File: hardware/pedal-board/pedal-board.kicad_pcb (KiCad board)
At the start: 2 copper layers, 108 x 64 mm, 50 parts, among them J1 AudioJack0, J10 CH7, J11 CH7, J12 Qwiic, J13 Qwiic, J2 AudioJack1, J3 AudioJack2, J4 AudioJack3, J5 Qwiic, J6 CH7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

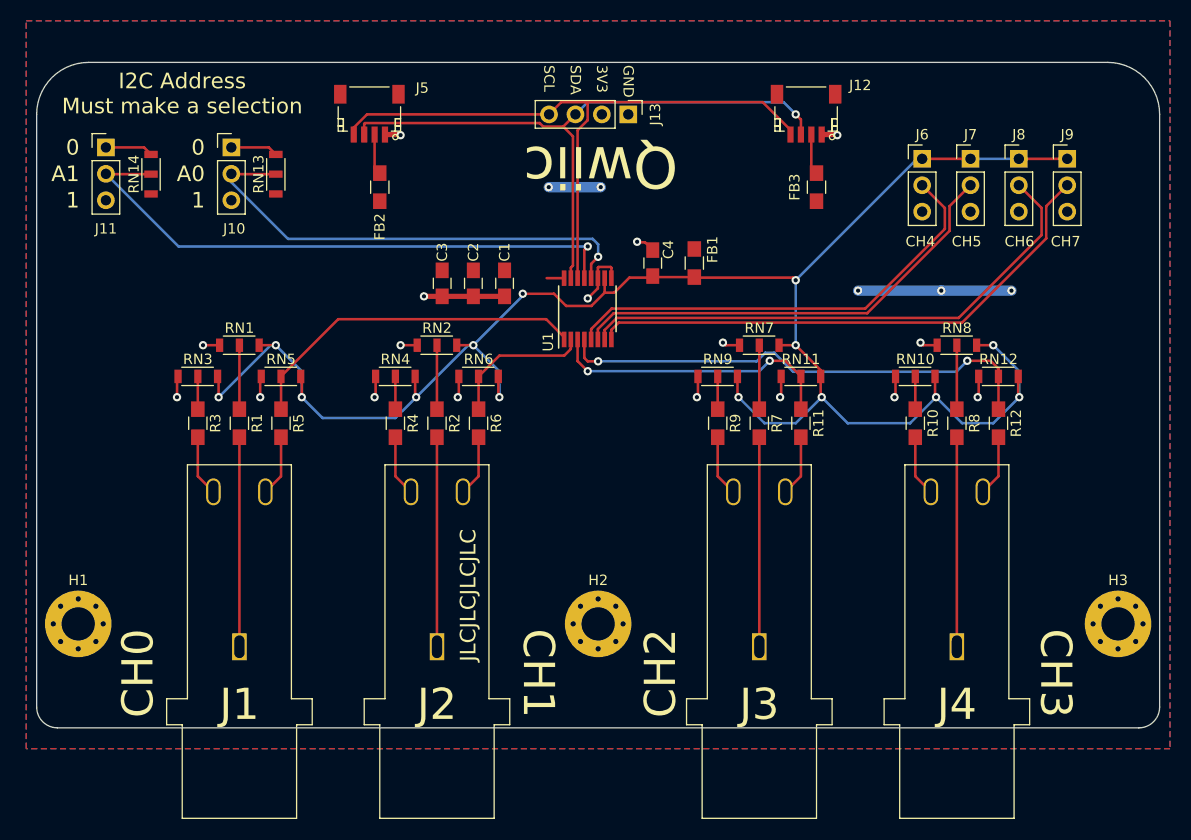
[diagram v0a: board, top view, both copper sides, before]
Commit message: Made changes for pedal board rev 2, per issue #40
* 1uF caps on all the incoming signal lines
* Switched to STM32G0 from the I2C ADC
* Added IRQ support, with transistor for pull down
* Every TRS pin is brought to an ADC pin, so we can attempt autodetection
  of pedal behavior.
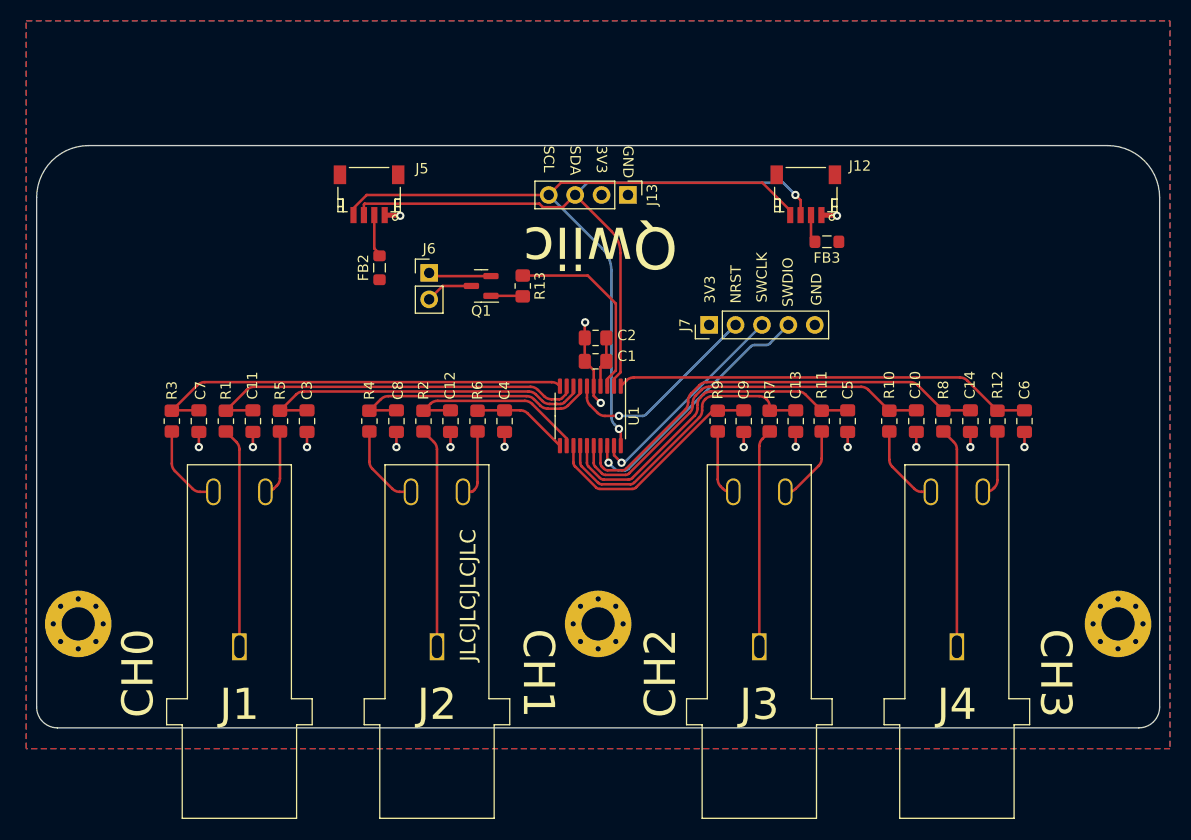
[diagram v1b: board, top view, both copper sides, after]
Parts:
- removed FB1: FB, Inductors_SMD:L_0805_HandSoldering
- removed J10, J11, J8, J9: CH7, Pin_Headers:Pin_Header_Straight_1x03_Pitch2.54mm
- removed RN1, RN10, RN11, RN12, RN13, RN14, RN2, RN3, RN4, RN5, RN6, RN7, RN8, RN9: Div, footprints:R_0805_Divider
- added C10: 1uF, Capacitor_SMD:C_0805_2012Metric_Pad1.18x1.45mm_HandSolder, F.Cu at (100.6, 68.5)
- added C11: 1uF, Capacitor_SMD:C_0805_2012Metric_Pad1.18x1.45mm_HandSolder, F.Cu at (36.8, 68.5)
- added C12: 1uF, Capacitor_SMD:C_0805_2012Metric_Pad1.18x1.45mm_HandSolder, F.Cu at (55.8, 68.5)
- added C13: 1uF, Capacitor_SMD:C_0805_2012Metric_Pad1.18x1.45mm_HandSolder, F.Cu at (89.0, 68.5)
- added C14: 1uF, Capacitor_SMD:C_0805_2012Metric_Pad1.18x1.45mm_HandSolder, F.Cu at (105.8, 68.5)
- added C5: 1uF, Capacitor_SMD:C_0805_2012Metric_Pad1.18x1.45mm_HandSolder, F.Cu at (94.0, 68.5)
- added C6: 1uF, Capacitor_SMD:C_0805_2012Metric_Pad1.18x1.45mm_HandSolder, F.Cu at (111.0, 68.5)
- added C7: 1uF, Capacitor_SMD:C_0805_2012Metric_Pad1.18x1.45mm_HandSolder, F.Cu at (31.6, 68.5)
- added C8: 1uF, Capacitor_SMD:C_0805_2012Metric_Pad1.18x1.45mm_HandSolder, F.Cu at (50.6, 68.5)
- added C9: 1uF, Capacitor_SMD:C_0805_2012Metric_Pad1.18x1.45mm_HandSolder, F.Cu at (84.0, 68.5)
- added Q1: Q_NPN_BEC, Package_TO_SOT_SMD:SOT-23, F.Cu at (58.8, 55.5)
- added R13: 10k, Resistor_SMD:R_0805_2012Metric_Pad1.20x1.40mm_HandSolder, F.Cu at (62.8, 55.5)
- C1: footprint Capacitors_SMD:C_0805_HandSoldering -> Capacitor_SMD:C_0805_2012Metric_Pad1.18x1.45mm_HandSolder
- C2: value 1uF -> 4.7uF; footprint Capacitors_SMD:C_0805_HandSoldering -> Capacitor_SMD:C_0805_2012Metric_Pad1.18x1.45mm_HandSolder
- C3: value 4.7uF -> 1uF; footprint Capacitors_SMD:C_0805_HandSoldering -> Capacitor_SMD:C_0805_2012Metric_Pad1.18x1.45mm_HandSolder
- C4: value 0.1uF -> 1uF; footprint Capacitors_SMD:C_0805_HandSoldering -> Capacitor_SMD:C_0805_2012Metric_Pad1.18x1.45mm_HandSolder
- FB2, FB3: footprint Inductors_SMD:L_0805_HandSoldering -> Inductor_SMD:L_0805_2012Metric_Pad1.05x1.20mm_HandSolder
- J13: footprint Pin_Headers:Pin_Header_Straight_1x04_Pitch2.54mm -> Connector_PinHeader_2.54mm:PinHeader_1x04_P2.54mm_Vertical
- J6: value CH7 -> IRQ; footprint Pin_Headers:Pin_Header_Straight_1x03_Pitch2.54mm -> Connector_PinHeader_2.54mm:PinHeader_1x02_P2.54mm_Vertical
- J7: value CH7 -> Serial Wire Debug; footprint Pin_Headers:Pin_Header_Straight_1x03_Pitch2.54mm -> Connector_PinHeader_2.54mm:PinHeader_1x05_P2.54mm_Vertical
- R1, R10, R11, R12, R2, R3, R4, R5, R6, R7, R8, R9: footprint Resistors_SMD:R_0805_HandSoldering -> Resistor_SMD:R_0805_2012Metric_Pad1.20x1.40mm_HandSolder
- U1: value ADS7830 -> STM32G030Fx; footprint Housings_SSOP:TSSOP-16_4.4x5mm_Pitch0.65mm -> Package_SO:TSSOP-20_4.4x6.5mm_P0.65mm
- moved J6 48.7 mm to (53.8, 54.2)
- moved J7 29.8 mm to (80.7, 59.2), turned to 90 degrees
- moved C4 20.8 mm to (61.0, 68.5), turned to -90 degrees
- moved C3 18.6 mm to (42.0, 68.5)
- moved C2 12.9 mm to (69.8, 60.5), turned to 180 degrees
- moved C1 11.5 mm to (69.8, 62.8), turned to 180 degrees
- moved U1 10.3 mm to (69.2, 68.0), turned to -90 degrees
- moved FB2 7.75 mm to (49.0, 53.8)
- moved J12 7.75 mm to (90.0, 46.8)
- moved J13 7.75 mm to (72.9, 46.8)
- moved J5 7.75 mm to (48.0, 46.8)
- moved FB3 5.34 mm to (92.0, 51.2), turned to 180 degrees
- moved R10 2.51 mm to (98.0, 68.5)
- moved R3 2.51 mm to (29.0, 68.5)
- moved R4 2.51 mm to (48.0, 68.5)
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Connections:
- net Net-(J7-Pad2) renamed /NRST
- C3 pad 1: +3V3 -> /J1_T
- C4 pad 1: +3.3VA -> /J2_T
- J6 pad 1: +3.3VA -> GND
- J7 pad 1: +3.3VA -> +3V3
- J7 pad 3: GND -> /SWCLK
- R1 pad 1: Net-(R1-Pad1) -> /J1_S
- R10 pad 1: Net-(R10-Pad1) -> /J4_R
- R11 pad 1: /CH2 -> /J3_T
- R12 pad 1: /CH3 -> /J4_T
- R2 pad 1: Net-(R2-Pad1) -> /J2_S
- R3 pad 1: Net-(R3-Pad1) -> /J1_R
- R4 pad 1: Net-(R4-Pad1) -> /J2_R
- R5 pad 1: /CH0 -> /J1_T
- R6 pad 1: /CH1 -> /J2_T
- R7 pad 1: Net-(R7-Pad1) -> /J3_S
- R8 pad 1: Net-(R8-Pad1) -> /J4_S
- R9 pad 1: Net-(R9-Pad1) -> /J3_R
- U1 pad 1: /CH0 -> /J4_T
- U1 pad 10: +3.3VA -> /J1_R
- U1 pad 11: GND -> /J2_T
- U1 pad 12: /A0 -> /J2_S
- U1 pad 13: /A1 -> /J3_R
- U1 pad 14: /SCL -> /J3_S
- U1 pad 15: /SDA -> /J3_T
- U1 pad 16: +3V3 -> /J4_R
- U1 pad 2: /CH1 -> /SDA
- U1 pad 3: /CH2 -> /IRQ
- U1 pad 4: /CH3 -> +3V3
- U1 pad 5: Net-(J6-Pad2) -> GND
- U1 pad 7: Net-(J8-Pad2) -> /J2_R
- U1 pad 8: Net-(J9-Pad2) -> /J1_T
- U1 pad 9: GND -> /J1_S
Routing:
- net +3.3VA: track 179.6 -> 0.00 mm, vias 14 -> 0
- net /A1: track 56.8 -> 0.00 mm, vias 1 -> 0
- net Net-(J8-Pad2): track 52.4 -> 0.00 mm
- net Net-(J9-Pad2): track 52.3 -> 0.00 mm
- net /CH3: track 47.5 -> 0.00 mm, vias 2 -> 0
- net /A0: track 46.4 -> 0.00 mm, vias 1 -> 0
- net /J4_S: track 0.00 -> 42.6 mm
- net /J1_R: track 0.00 -> 41.1 mm
- net /J4_T: track 0.00 -> 40.4 mm
- net Net-(J6-Pad2): track 44.1 -> 4.60 mm
- net /J4_R: track 0.00 -> 38.1 mm
- net /J1_S: track 0.00 -> 37.6 mm
- net /CH0: track 33.6 -> 0.00 mm
- net /J1_T: track 0.00 -> 33.0 mm
- net /J3_T: track 0.00 -> 32.2 mm
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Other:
- board size 108 x 64 mm -> 108 x 56 mm
- net class Default removed
- board text added: "NRST"
- board text added: "Pedal board 1/4{dblquote} TRS jacks - Rev2α http://github.com/jkominek/piano-conversion"
- board text added: "SWCLK"
- board text added: "SWDIO"
- board text removed: "0"
- board text removed: "1"
- board text removed: "A0"
- board text removed: "A1"
- board text removed: "CH4"
- board text removed: "CH5"
- board text removed: "CH6"
- board text removed: "CH7"
- board text removed: "I2C Address Must make a selection"
- board text removed: "Pedal board 1/4" TRS jacks - Rev1 http://github.com/jkominek/piano-conversion"

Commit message: Brought out all ADC lines, and put some power on adjacent pins
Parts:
- added J10: Conn_01x04_Male, Connector_PinHeader_2.54mm:PinHeader_1x04_P2.54mm_Vertical, F.Cu at (27.0, 47.6)
- added J8: Conn_01x04_Male, Connector_PinHeader_2.54mm:PinHeader_1x04_P2.54mm_Vertical, F.Cu at (22.0, 47.6)
- added J9: ADC Lines, Connector_PinHeader_2.54mm:PinHeader_1x12_P2.54mm_Vertical, F.Cu at (24.5, 47.6)
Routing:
- net /J4_T: track 40.4 -> 95.9 mm, vias 0 -> 1
- net /J4_S: track 42.6 -> 95.8 mm, vias 0 -> 1
- net /J4_R: track 38.1 -> 86.1 mm, vias 0 -> 1
- net /J3_T: track 32.2 -> 80.1 mm, vias 0 -> 1
- net /J3_S: track 28.3 -> 76.0 mm, vias 0 -> 1
- net /J3_R: track 22.2 -> 69.4 mm, vias 0 -> 1
- net /J2_T: track 9.30 -> 53.6 mm, vias 0 -> 1
- net /J2_S: track 18.9 -> 56.8 mm, vias 0 -> 1
- net GND: track 35.0 -> 69.0 mm, vias 16 -> 21
- net /J2_R: track 25.1 -> 57.6 mm, vias 0 -> 1
- net /J1_T: track 33.0 -> 57.3 mm, vias 0 -> 1
- net /J1_S: track 37.6 -> 53.7 mm, vias 0 -> 1
- net /J1_R: track 41.1 -> 50.5 mm, vias 0 -> 1
- net +3V3: track 4.87 -> 12.5 mm
- net /SCL: track 72.0 -> 69.0 mm, vias 1 -> 2

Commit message: Convert all other mounting holes to non-pad variety.
Reroute a few traces to be shorter.
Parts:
- H1, H2, H3: footprint Mounting_Holes:MountingHole_3.2mm_M3_Pad_Via -> MountingHole:MountingHole_3.2mm_M3
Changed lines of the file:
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@@
       (net 15 "/SCL") (pinfunction "Pin_4") (pintype "passive"))
   )
-  (footprint "Mounting_Holes:MountingHole_3.2mm_M3_Pad_Via" (layer "F.Cu")
+  (footprint "MountingHole:MountingHole_3.2mm_M3" (layer "F.Cu")
     (at 20 88)
-    (descr "Mounting Hole 3.2mm, M3")
-    (tags "mounting hole 3.2mm m3")
+    (descr "Mounting Hole 3.2mm, no annular, M3")
+    (tags "mounting hole 3.2mm no annular m3")
     (property "Sheetfile" "pedal-board.kicad_sch")
     (property "Sheetname" "")
@@
     (fp_circle (center 0 0) (end 3.2 0) (layer "Cmts.User") (width 0.15) (fill none))
     (fp_circle (center 0 0) (end 3.45 0) (layer "F.CrtYd") (width 0.05) (fill none))
-    (pad "1" thru_hole circle locked (at 1.697056 1.697056) (size 0.8 0.8) (drill 0.5) (layers *.Cu *.Mask)
-      (net 1 "GND") (pinfunction "1") (pintype "input"))
-    (pad "1" thru_hole circle locked (at 2.4 0) (size 0.8 0.8) (drill 0.5) (layers *.Cu *.Mask)
-      (net 1 "GND") (pinfunction "1") (pintype "input"))
-    (pad "1" thru_hole circle locked (at 0 2.4) (size 0.8 0.8) (drill 0.5) (layers *.Cu *.Mask)
-      (net 1 "GND") (pinfunction "1") (pintype "input"))
-    (pad "1" thru_hole circle locked (at 1.697056 -1.697056) (size 0.8 0.8) (drill 0.5) (layers *.Cu *.Mask)
-      (net 1 "GND") (pinfunction "1") (pintype "input"))
-    (pad "1" thru_hole circle locked (at -1.697056 -1.697056) (size 0.8 0.8) (drill 0.5) (layers *.Cu *.Mask)
-      (net 1 "GND") (pinfunction "1") (pintype "input"))
-    (pad "1" thru_hole circle locked (at 0 -2.4) (size 0.8 0.8) (drill 0.5) (layers *.Cu *.Mask)
-      (net 1 "GND") (pinfunction "1") (pintype "input"))
-    (pad "1" thru_hole circle locked (at 0 0) (size 6.4 6.4) (drill 3.2) (layers *.Cu *.Mask)
-      (net 1 "GND") (pinfunction "1") (pintype "input"))
-    (pad "1" thru_hole circle locked (at -1.697056 1.697056) (size 0.8 0.8) (drill 0.5) (layers *.Cu *.Mask)
-      (net 1 "GND") (pinfunction "1") (pintype "input"))
-    (pad "1" thru_hole circle locked (at -2.4 0) (size 0.8 0.8) (drill 0.5) (layers *.Cu *.Mask)
-      (net 1 "GND") (pinfunction "1") (pintype "input"))
+    (pad "" np_thru_hole circle locked (at 0 0) (size 3.2 3.2) (drill 3.2) (layers *.Cu *.Mask))
   )
-  (footprint "Mounting_Holes:MountingHole_3.2mm_M3_Pad_Via" (layer "F.Cu")
+  (footprint "MountingHole:MountingHole_3.2mm_M3" (layer "F.Cu")
     (at 70 88)
-    (descr "Mounting Hole 3.2mm, M3")
-    (tags "mounting hole 3.2mm m3")
+    (descr "Mounting Hole 3.2mm, no annular, M3")
+    (tags "mounting hole 3.2mm no annular m3")
     (property "Sheetfile" "pedal-board.kicad_sch")
     (property "Sheetname" "")
@@
     (fp_circle (center 0 0) (end 3.2 0) (layer "Cmts.User") (width 0.15) (fill none))
     (fp_circle (center 0 0) (end 3.45 0) (layer "F.CrtYd") (width 0.05) (fill none))
-    (pad "1" thru_hole circle locked (at -1.697056 1.697056) (size 0.8 0.8) (drill 0.5) (layers *.Cu *.Mask)
-      (net 1 "GND") (pinfunction "1") (pintype "input"))
-    (pad "1" thru_hole circle locked (at 0 0) (size 6.4 6.4) (drill 3.2) (layers *.Cu *.Mask)
-      (net 1 "GND") (pinfunction "1") (pintype "input"))
-    (pad "1" thru_hole circle locked (at -2.4 0) (size 0.8 0.8) (drill 0.5) (layers *.Cu *.Mask)
-      (net 1 "GND") (pinfunction "1") (pintype "input"))
-    (pad "1" thru_hole circle locked (at -1.697056 -1.697056) (size 0.8 0.8) (drill 0.5) (layers *.Cu *.Mask)
-      (net 1 "GND") (pinfunction "1") (pintype "input"))
-    (pad "1" thru_hole circle locked (at 1.697056 -1.697056) (size 0.8 0.8) (drill 0.5) (layers *.Cu *.Mask)
-      (net 1 "GND") (pinfunction "1") (pintype "input"))
-    (pad "1" thru_hole circle locked (at 1.697056 1.697056) (size 0.8 0.8) (drill 0.5) (layers *.Cu *.Mask)
-      (net 1 "GND") (pinfunction "1") (pintype "input"))
-    (pad "1" thru_hole circle locked (at 0 2.4) (size 0.8 0.8) (drill 0.5) (layers *.Cu *.Mask)
-      (net 1 "GND") (pinfunction "1") (pintype "input"))
-    (pad "1" thru_hole circle locked (at 0 -2.4) (size 0.8 0.8) (drill 0.5) (layers *.Cu *.Mask)
-      (net 1 "GND") (pinfunction "1") (pintype "input"))
-    (pad "1" thru_hole circle locked (at 2.4 0) (size 0.8 0.8) (drill 0.5) (layers *.Cu *.Mask)
-      (net 1 "GND") (pinfunction "1") (pintype "input"))
+    (pad "" np_thru_hole circle locked (at 0 0) (size 3.2 3.2) (drill 3.2) (layers *.Cu *.Mask))
   )
-  (footprint "Mounting_Holes:MountingHole_3.2mm_M3_Pad_Via" (layer "F.Cu")
+  (footprint "MountingHole:MountingHole_3.2mm_M3" (layer "F.Cu")
     (at 120 88)
-    (descr "Mounting Hole 3.2mm, M3")
-    (tags "mounting hole 3.2mm m3")
+    (descr "Mounting Hole 3.2mm, no annular, M3")
+    (tags "mounting hole 3.2mm no annular m3")
     (property "Sheetfile" "pedal-board.kicad_sch")
     (property "Sheetname" "")
@@
     (fp_circle (center 0 0) (end 3.2 0) (layer "Cmts.User") (width 0.15) (fill none))
     (fp_circle (center 0 0) (end 3.45 0) (layer "F.CrtYd") (width 0.05) (fill none))
-    (pad "1" thru_hole circle locked (at 0 2.4) (size 0.8 0.8) (drill 0.5) (layers *.Cu *.Mask)
-      (net 1 "GND") (pinfunction "1") (pintype "input"))
-    (pad "1" thru_hole circle locked (at -1.697056 1.697056) (size 0.8 0.8) (drill 0.5) (layers *.Cu *.Mask)
-      (net 1 "GND") (pinfunction "1") (pintype "input"))
-    (pad "1" thru_hole circle locked (at 0 0) (size 6.4 6.4) (drill 3.2) (layers *.Cu *.Mask)
-      (net 1 "GND") (pinfunction "1") (pintype "input"))
-    (pad "1" thru_hole circle locked (at -1.697056 -1.697056) (size 0.8 0.8) (drill 0.5) (layers *.Cu *.Mask)
-      (net 1 "GND") (pinfunction "1") (pintype "input"))
-    (pad "1" thru_hole circle locked (at 0 -2.4) (size 0.8 0.8) (drill 0.5) (layers *.Cu *.Mask)
-      (net 1 "GND") (pinfunction "1") (pintype "input"))
-    (pad "1" thru_hole circle locked (at 1.697056 -1.697056) (size 0.8 0.8) (drill 0.5) (layers *.Cu *.Mask)
-      (net 1 "GND") (pinfunction "1") (pintype "input"))
-    (pad "1" thru_hole circle locked (at 2.4 0) (size 0.8 0.8) (drill 0.5) (layers *.Cu *.Mask)
-      (net 1 "GND") (pinfunction "1") (pintype "input"))
-    (pad "1" thru_hole circle locked (at -2.4 0) (size 0.8 0.8) (drill 0.5) (layers *.Cu *.Mask)
-      (net 1 "GND") (pinfunction "1") (pintype "input"))
-    (pad "1" thru_hole circle locked (at 1.697056 1.697056) (size 0.8 0.8) (drill 0.5) (layers *.Cu *.Mask)
-      (net 1 "GND") (pinfunction "1") (pintype "input"))
+    (pad "" np_thru_hole circle locked (at 0 0) (size 3.2 3.2) (drill 3.2) (layers *.Cu *.Mask))
   )
   (footprint "Connector_PinHeader_2.54mm:PinHeader_1x04_P2.54mm_Vertical" (layer "F.Cu")

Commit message: Next revs of the important boards
Includes some tiny DRC tweaks for the LED power board.
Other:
- board text added: "Pedal board 1/4{dblquote} TRS jacks - Rev2 http://github.com/jkominek/piano-conversion"
- board text removed: "Pedal board 1/4{dblquote} TRS jacks - Rev2α http://github.com/jkominek/piano-conversion"
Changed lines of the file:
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@@
   (gr_line (start 119 42) (end 21 42) (layer "Edge.Cuts") (width 0.05))
   (gr_line (start 18 98) (end 122 98) (layer "Edge.Cuts") (width 0.05))
-  (gr_text "Pedal board 1/4{dblquote} TRS jacks - Rev2α\nhttp://github.com/jkominek/piano-conversion" (at 70 52.75) (layer "B.SilkS")
+  (gr_text "Pedal board 1/4{dblquote} TRS jacks - Rev2\nhttp://github.com/jkominek/piano-conversion" (at 70 52.75) (layer "B.SilkS")
     (effects (font (size 1.5 1.5) (thickness 0.2)) (justify mirror))
   )
